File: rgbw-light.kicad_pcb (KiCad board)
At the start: 2 copper layers, 26 x 26 mm, 22 parts, among them IC1 PAM2804AAB010, IC2 PAM2804AAB010, IC3 PAM2804AAB010, IC4 PAM2804AAB010

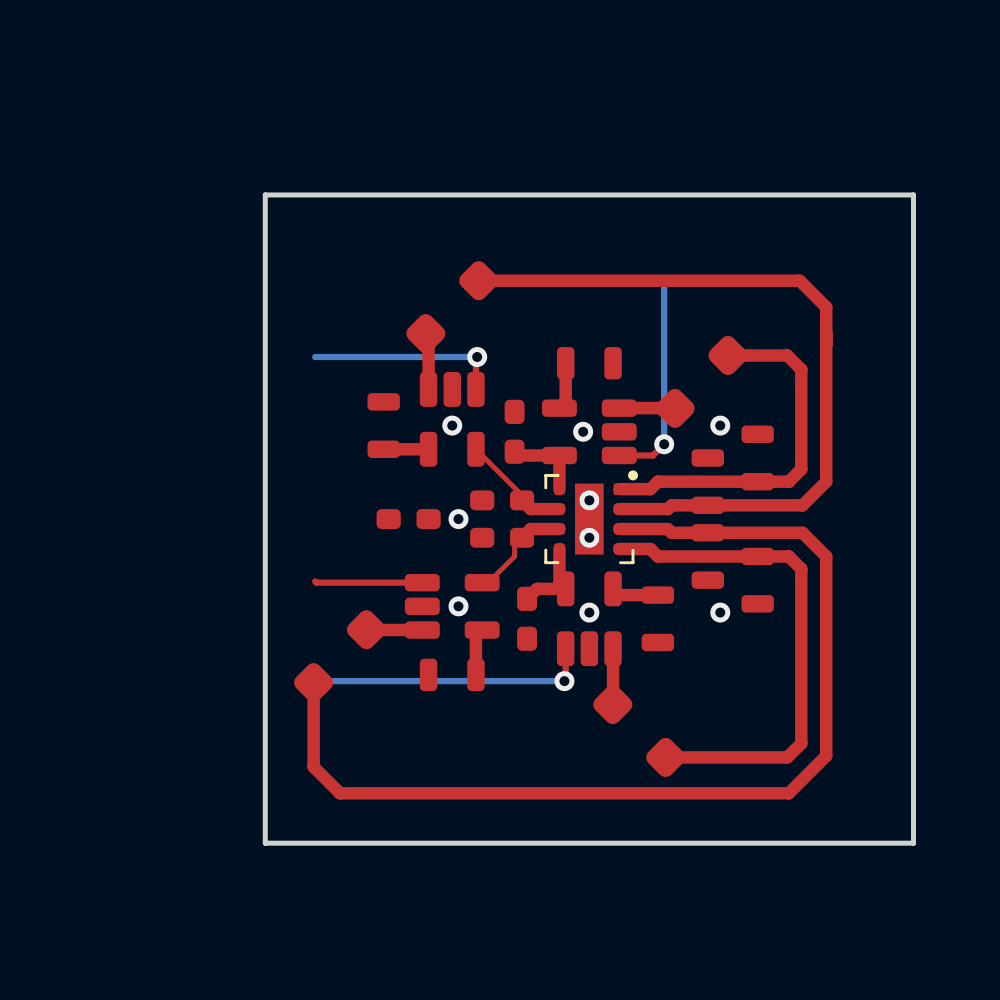
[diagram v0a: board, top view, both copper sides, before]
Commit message: added connector, mounting holes. completed layout
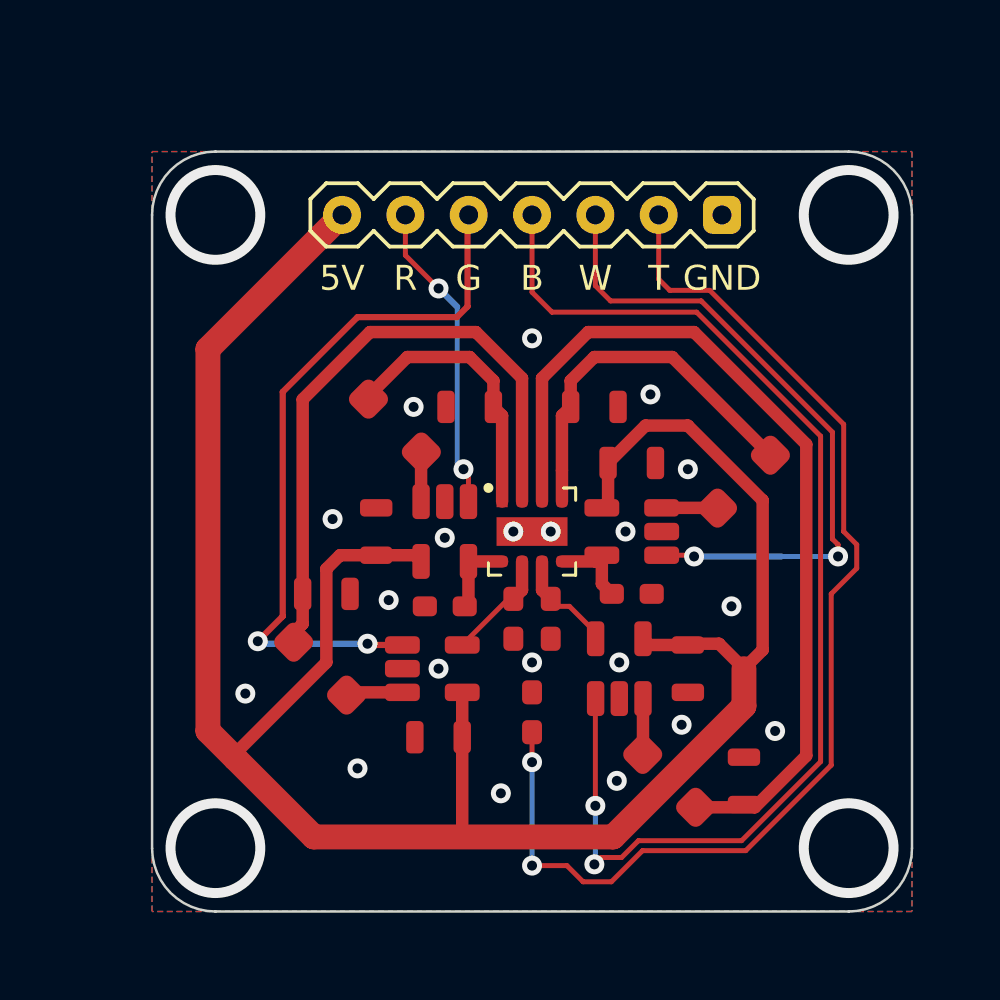
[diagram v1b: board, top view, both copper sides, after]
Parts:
- added CN1: 1x7, pin_headers:1x7, F.Cu at (145.2, 83.3)
- moved C4 15.9 mm to (136.9, 98.5), turned to 0 degrees
- moved L2 15.4 mm to (136.7, 101.5), turned to 180 degrees
- moved L3 14.1 mm to (150.7, 106.0), turned to 0 degrees
- moved C3 12.7 mm to (141.4, 104.2), turned to 180 degrees
- moved L1 12.4 mm to (139.7, 91.8), turned to 180 degrees
- moved C2 11.7 mm to (142.7, 91.0), turned to 180 degrees
- moved C1 10.9 mm to (138.9, 96.0), turned to 90 degrees
- moved L4 10.8 mm to (153.7, 94.0), turned to 90 degrees
- moved IC2 10.0 mm to (141.2, 101.5), turned to 0 degrees
- moved C8 9.55 mm to (147.7, 91.0), turned to 0 degrees
- moved C5 9.45 mm to (151.4, 101.5), turned to -90 degrees
- moved NTC1 9.20 mm to (145.2, 103.2), turned to -90 degrees
- moved C6 9.12 mm to (153.7, 106.0), turned to 90 degrees
- moved R1 7.54 mm to (141.7, 99.0), turned to 0 degrees
- moved IC3 7.15 mm to (148.7, 101.5), turned to 90 degrees
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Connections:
- D1 pad 0: (no net) -> GND
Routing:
- net 5V: track 7.51 -> 90.5 mm
- net /Temperature: track 0.00 -> 46.3 mm, vias 0 -> 2
- net /B: track 4.32 -> 47.6 mm, vias 0 -> 2
- net /G: track 7.82 -> 28.8 mm, vias 1 -> 2
- net /W: track 10.8 -> 30.5 mm, vias 1 -> 2
- net Net-(C6-Pad1): track 41.8 -> 36.0 mm
- net Net-(C8-Pad1): track 20.3 -> 15.0 mm
- net Net-(C4-Pad1): track 30.6 -> 25.5 mm
- net /R: track 8.49 -> 12.6 mm, vias 1 -> 2
- net Net-(C2-Pad1): track 15.1 -> 11.4 mm
- net GND: vias 9 -> 24
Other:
- board size 26 x 26 mm -> 30.5 x 30.5 mm
- board text added: "5V"
- board text added: "B"
- board text added: "G"
- board text added: "GND"
- board text added: "R"
- board text added: "T"
- board text added: "W"

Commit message: minor cleanup. generated outputs
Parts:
- moved C2 0.30 mm to (143.0, 91.0)
- moved C8 0.30 mm to (147.4, 91.0)
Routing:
- net Net-(D1-Pad7): track 4.46 -> 4.99 mm
- net Net-(C4-Pad1): track 25.5 -> 25.0 mm
- net GND: vias 24 -> 25

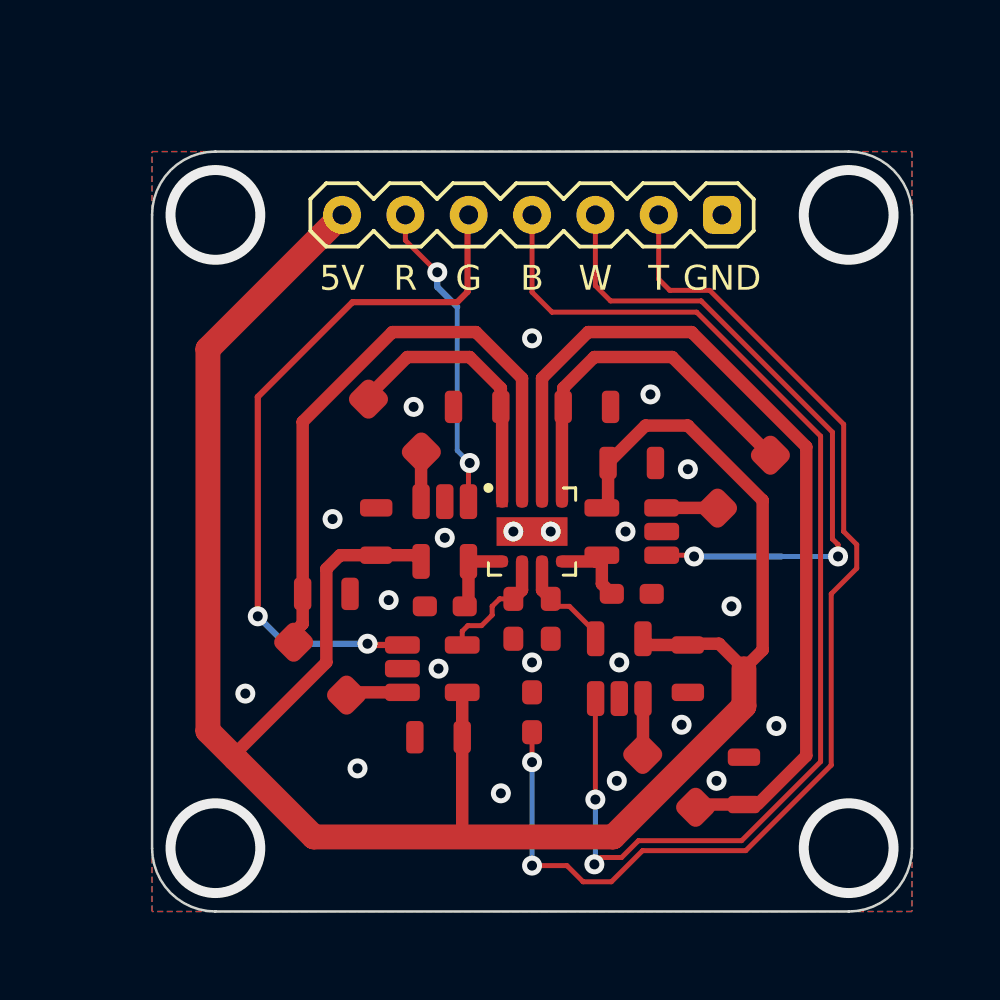
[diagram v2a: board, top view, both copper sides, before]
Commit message: changed layout to match d1 mini
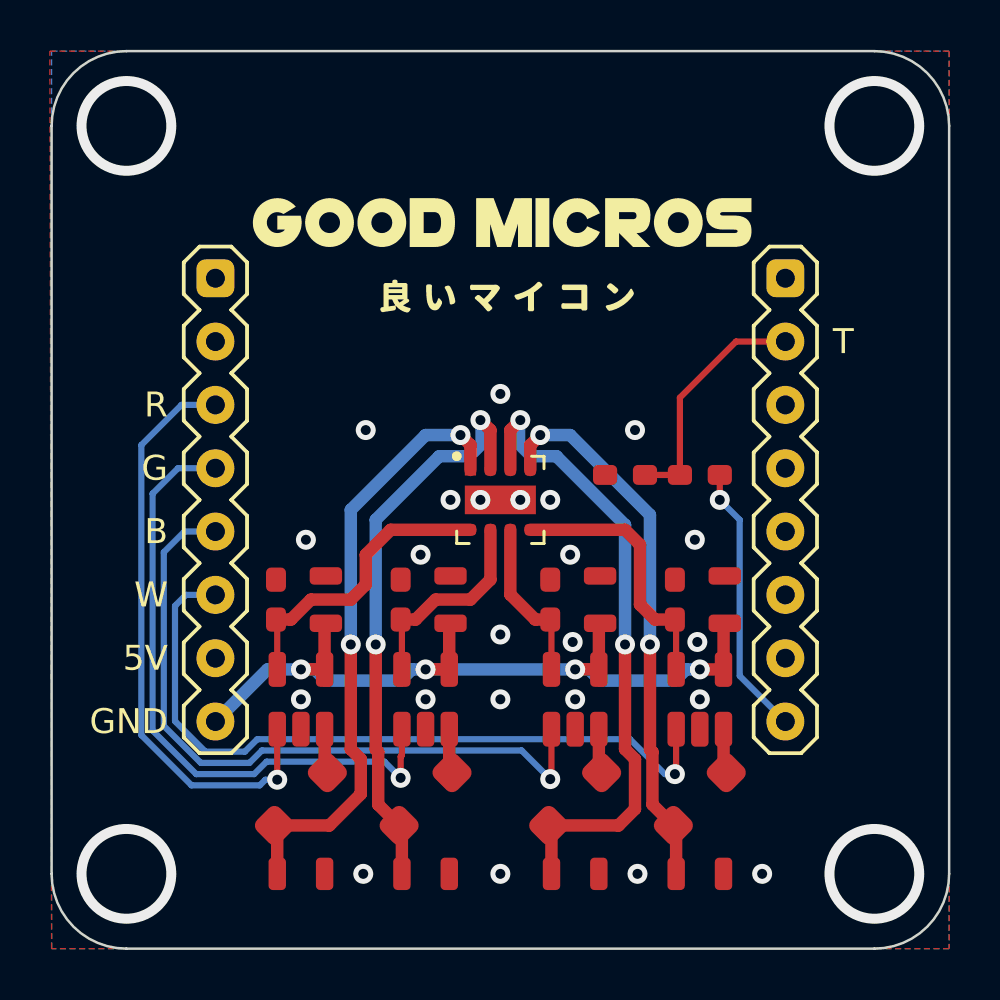
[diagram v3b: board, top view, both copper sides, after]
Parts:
- added CN2: 1x8, pin_headers:1x8, F.Cu at (155.4, 93.5)
- added R5: 10k, SMT:0603, F.Cu at (151.9, 93.7)
- CN1: value 1x7 -> 1x8; footprint pin_headers:1x7 -> pin_headers:1x8
- moved C2 20.0 mm to (135.9, 109.7), turned to 0 degrees
- moved C8 19.3 mm to (151.9, 109.7)
- moved CN1 16.3 mm to (132.5, 93.5), turned to 0 degrees
- moved L1 15.4 mm to (135.9, 106.7), turned to -90 degrees
- moved L4 12.9 mm to (151.9, 106.7), turned to -90 degrees
- moved C4 11.9 mm to (140.9, 109.7)
- moved NTC1 10.2 mm to (148.9, 93.7), turned to 0 degrees
- moved IC1 8.86 mm to (135.9, 102.7), turned to 90 degrees
- moved C6 7.73 mm to (146.9, 109.7), turned to 0 degrees
- moved IC4 7.26 mm to (151.9, 102.7), turned to 90 degrees
- moved R1 6.78 mm to (134.9, 98.7), turned to -90 degrees
- moved L2 6.73 mm to (140.9, 106.7), turned to -90 degrees
- moved C7 6.63 mm to (152.9, 98.7), turned to 90 degrees
- moved C3 5.54 mm to (141.9, 98.7), turned to 90 degrees
- moved R2 4.59 mm to (139.9, 98.7), turned to -90 degrees
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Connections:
- CN1 pad 1: GND -> unconnected-(CN1-Pad1)
- CN1 pad 2: /Temperature -> unconnected-(CN1-Pad2)
- CN1 pad 3: /W -> /R
- CN1 pad 4: /B -> /G
- CN1 pad 5: /G -> /B
- CN1 pad 6: /R -> /W
- CN1 pad 7: 5V -> GND
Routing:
- net 5V: track 90.5 -> 32.3 mm, vias 0 -> 4
- net /Temperature: track 46.3 -> 9.66 mm, vias 2 -> 0
- net /B: track 47.6 -> 28.2 mm, vias 2 -> 1
- net Net-(D1A-A): track 11.4 -> 24.7 mm, vias 0 -> 2
- net /R: track 12.6 -> 23.7 mm, vias 2 -> 1
- net Net-(CN2-Pad8): track 0.00 -> 11.0 mm, vias 0 -> 1
- net Net-(D1C-A): track 35.9 -> 26.0 mm, vias 0 -> 2
- net Net-(D1A-K): track 3.21 -> 12.0 mm
- net Net-(D1D-K): track 3.42 -> 10.7 mm
- net Net-(D1D-A): track 15.0 -> 22.1 mm, vias 0 -> 2
- net Net-(D1B-K): track 4.99 -> 8.28 mm
- net /G: track 28.3 -> 25.6 mm, vias 2 -> 1
- net Net-(D1C-K): track 4.25 -> 6.63 mm
- net Net-(D1B-A): track 25.0 -> 23.3 mm, vias 0 -> 2
- net /W: track 30.5 -> 29.6 mm, vias 2 -> 1
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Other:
- board size 30.5 x 30.5 mm -> 36 x 36 mm
